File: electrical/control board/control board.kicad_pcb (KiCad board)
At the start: 4 copper layers, 72.4 x 149.8 mm, 57 parts, among them J1 analog_extra, J10 Motor_2, J11 Motor_3, J12 Motor_4, J13 Motor_5, J14 Motor_6, J15 Motor_7, J16 Motor_8, J2 Programming_Header, J3 Conn_01x08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

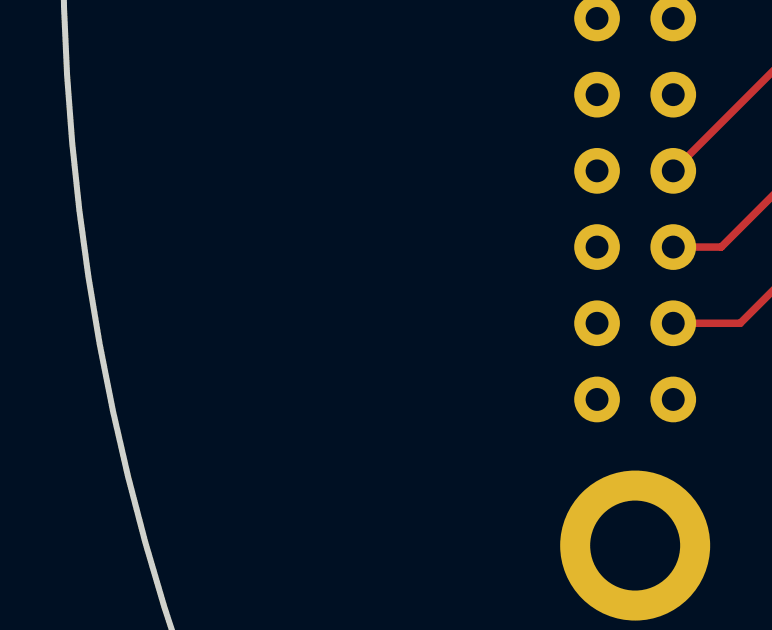
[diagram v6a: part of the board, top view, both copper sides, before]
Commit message: added low side switches to control board power
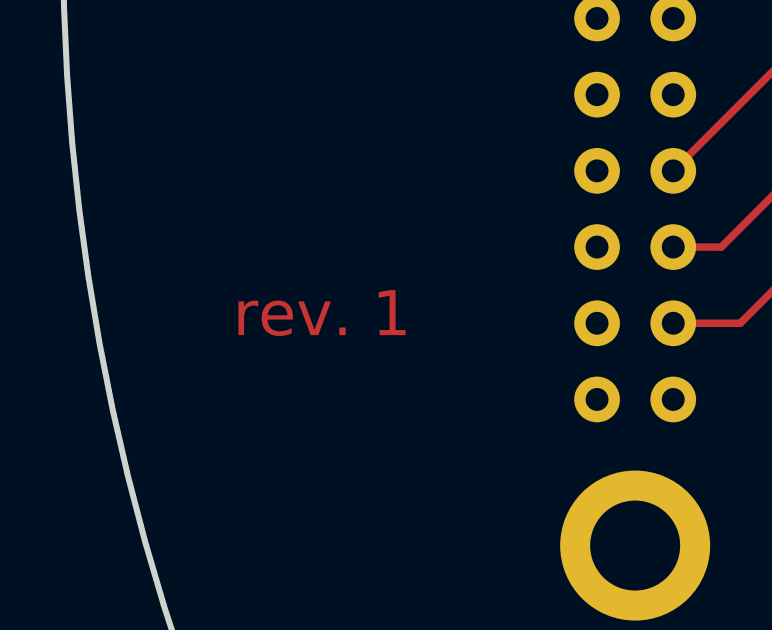
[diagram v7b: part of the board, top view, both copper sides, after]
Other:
- board text added: "rev. 1"
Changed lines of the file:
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@@
   (general
     (thickness 1.6)
-    (drawings 2)
+    (drawings 3)
     (tracks 488)
     (zones 0)
@@
     )
   )
+  (gr_text "rev. 1" (at 39.37 106.68) (layer F.Cu)
+    (effects (font (size 1.5 1.5) (thickness 0.3)))
+  )
   (gr_arc (start 105.664 94.190937) (end 103.124 19.304) (angle -176.1147961) (layer Edge.Cuts) (width 0.2))
   (gr_line (start 103.124 19.304) (end 103.124 169.077874) (layer Edge.Cuts) (width 0.2))
   (via (at 100.076 109.728) (size 0.8) (drill 0.4) (layers F.Cu B.Cu) (net 1))
   (via (at 98.044 105.918) (size 0.8) (drill 0.4) (layers F.Cu B.Cu) (net 1))
-  (via (at 67.056 68.072) (size 0.8) (drill 0.4) (layers F.Cu B.Cu) (net 2))
-  (via (at 57.15 113.919) (size 0.8) (drill 0.4) (layers F.Cu B.Cu) (net 2))
   (via (at 65.278 101.854) (size 0.8) (drill 0.4) (layers F.Cu B.Cu) (net 1))
   (via (at 65.024 95.25) (size 0.8) (drill 0.4) (layers F.Cu B.Cu) (net 1))
@@
   (via (at 79.133109 114.739942) (size 0.8) (drill 0.4) (layers F.Cu B.Cu) (net 1) (status 30))
   (via (at 79.133109 118.704942) (size 0.8) (drill 0.4) (layers F.Cu B.Cu) (net 1) (status 30))
-  (via (at 76.454 66.802) (size 0.8) (drill 0.4) (layers F.Cu B.Cu) (net 2) (status 30))
   (via (at 72.483109 123.952) (size 0.8) (drill 0.4) (layers F.Cu B.Cu) (net 1))
   (segment (start 72.708109 122.245942) (end 72.708109 123.727) (width 0.25) (layer B.Cu) (net 1))
@@
   (segment (start 97.145 109.357) (end 97.98099 108.52101) (width 0.2) (layer B.Cu) (net 1))
   (segment (start 97.98099 108.52101) (end 99.25099 108.52101) (width 0.2) (layer B.Cu) (net 1))
+  (via (at 67.056 68.072) (size 0.8) (drill 0.4) (layers F.Cu B.Cu) (net 2))
+  (via (at 57.15 113.919) (size 0.8) (drill 0.4) (layers F.Cu B.Cu) (net 2))
+  (via (at 76.454 66.802) (size 0.8) (drill 0.4) (layers F.Cu B.Cu) (net 2) (status 30))
   (via (at 72.644 58.547) (size 0.8) (drill 0.4) (layers F.Cu B.Cu) (net 2) (status 30))
   (segment (start 82.408109 120.295942) (end 81.658109 120.295942) (width 0.25) (layer B.Cu) (net 2) (status 30))

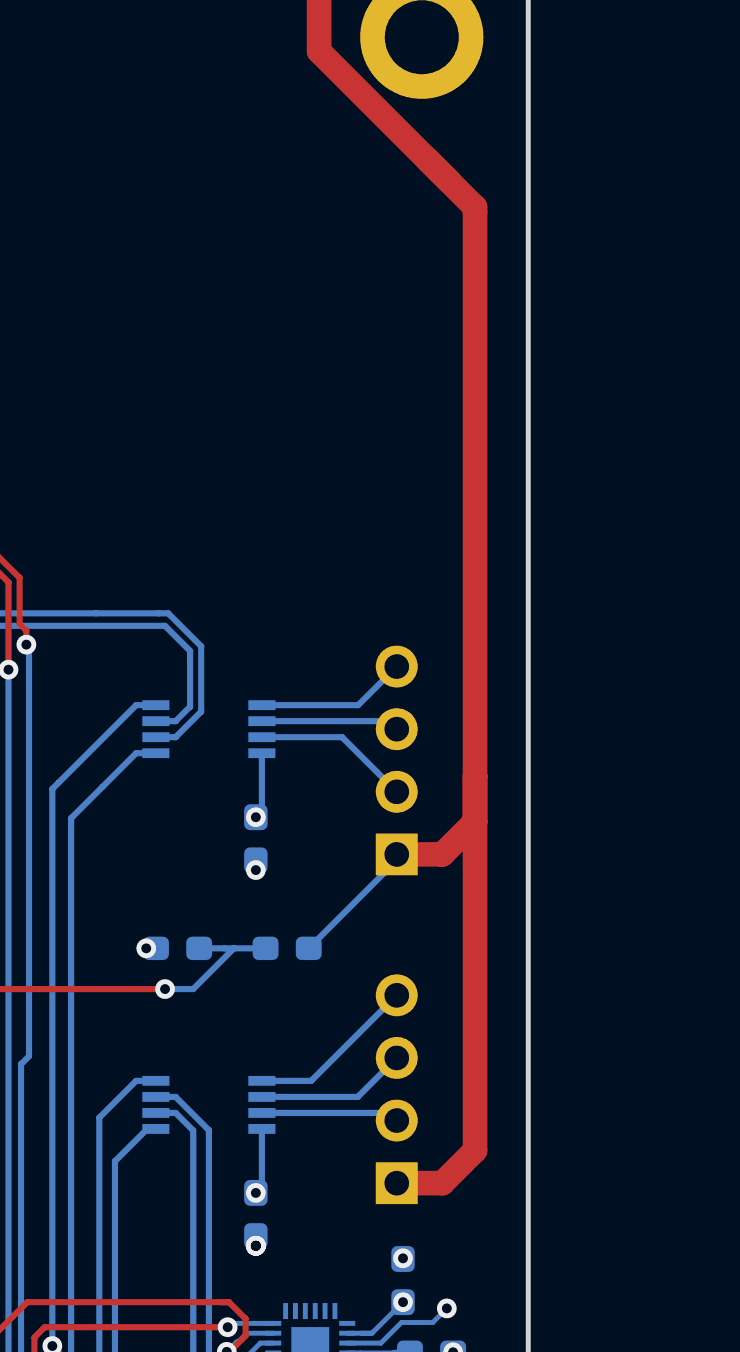
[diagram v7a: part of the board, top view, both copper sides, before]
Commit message: replaced the footprints of the data headers
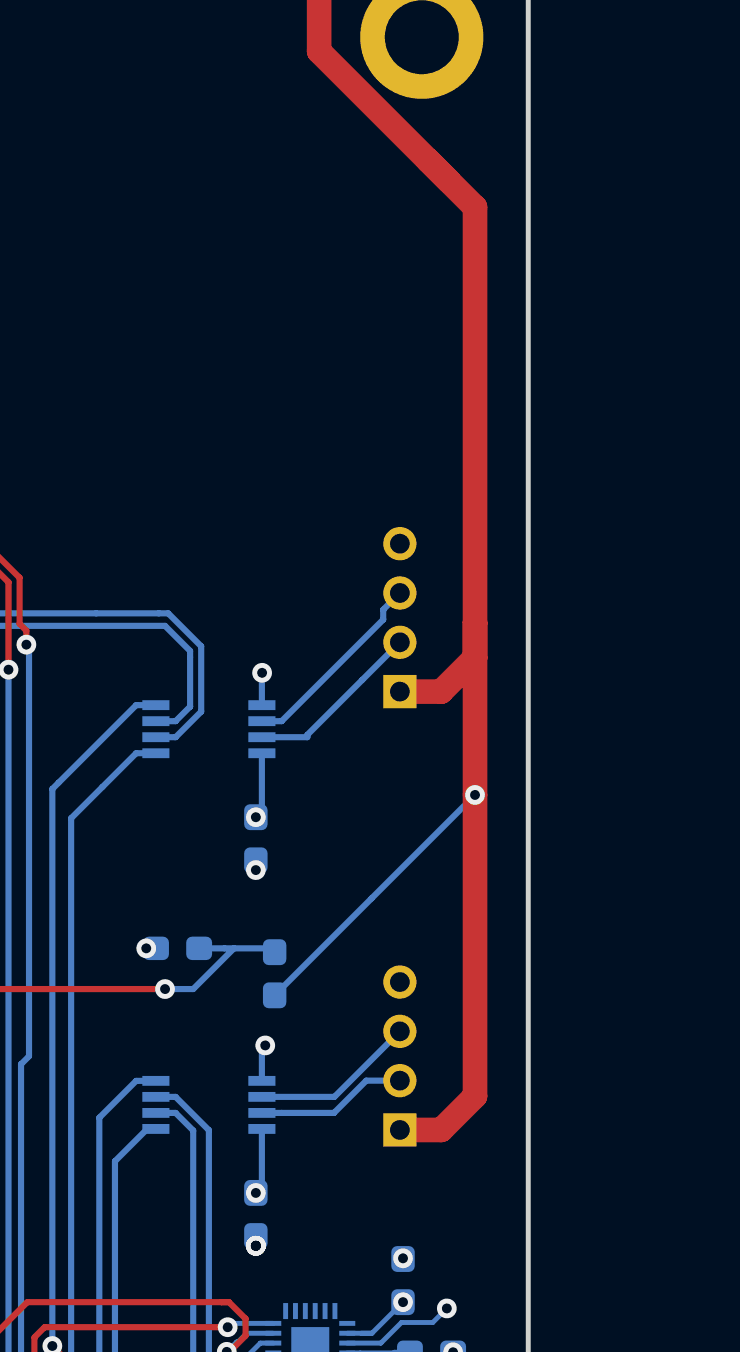
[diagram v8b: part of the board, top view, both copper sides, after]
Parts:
- C15, C17, C18: value .1uF -> 0.1uF
- J4, J6: footprint Connector_PinHeader_2.54mm:PinHeader_1x04_P2.54mm_Vertical -> Connector_Harwin:Harwin_LTek-Male_04_P2.00mm_Vertical
- moved J6 6.61 mm to (97.9, 82.9), turned to 90 degrees
- moved J4 2.16 mm to (97.9, 100.7), turned to 90 degrees
- moved R15 1.15 mm to (92.8, 94.4), turned to 90 degrees
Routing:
- net GND: track 39.1 -> 28.9 mm, vias 31 -> 33
- net +48V: track 79.4 -> 82.7 mm, vias 0 -> 1
- net Net-(J6-Pad3): track 5.60 -> 7.99 mm
- net Net-(J6-Pad2): track 6.39 -> 7.25 mm
- net Net-(J4-Pad3): track 6.12 -> 6.70 mm
- net Net-(J4-Pad2): track 5.60 -> 6.14 mm
